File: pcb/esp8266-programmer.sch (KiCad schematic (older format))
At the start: 15 parts, among them P1 USB_OTG, P2 CONN_01X04, SW1 RESET, SW2 FLASH, SW3 SW_DP3T, U1 MCP1700T-3302E/TT, U1 MCP2221-I/SL

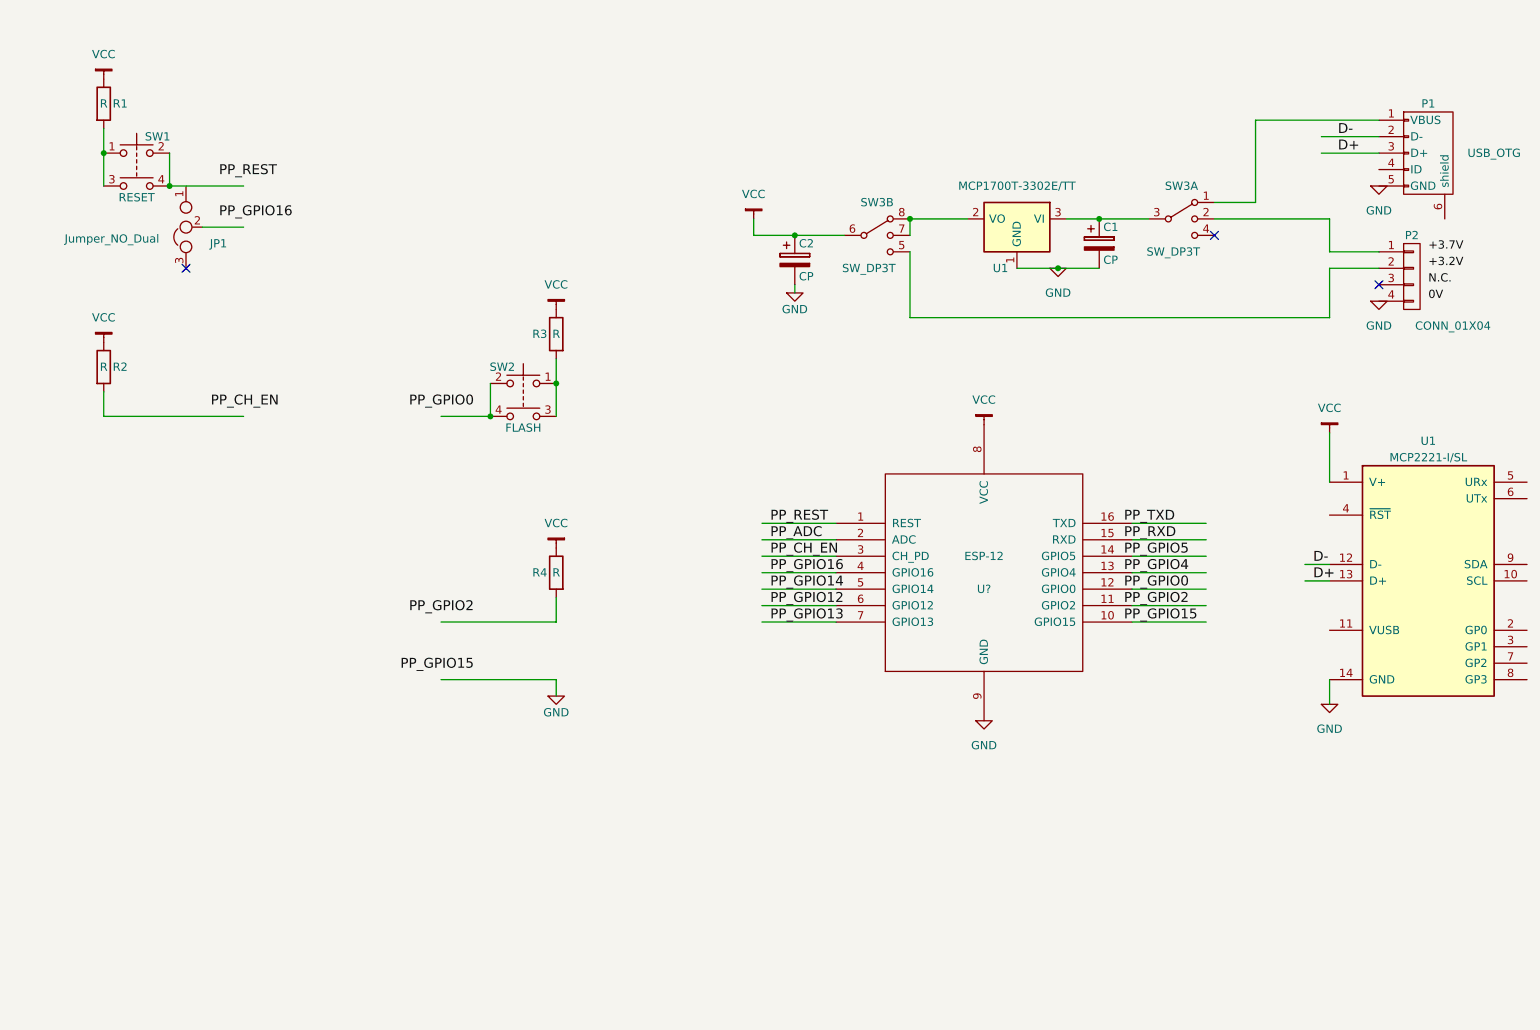
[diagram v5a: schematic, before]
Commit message: Fix wiring for switches. Add GPIO conns
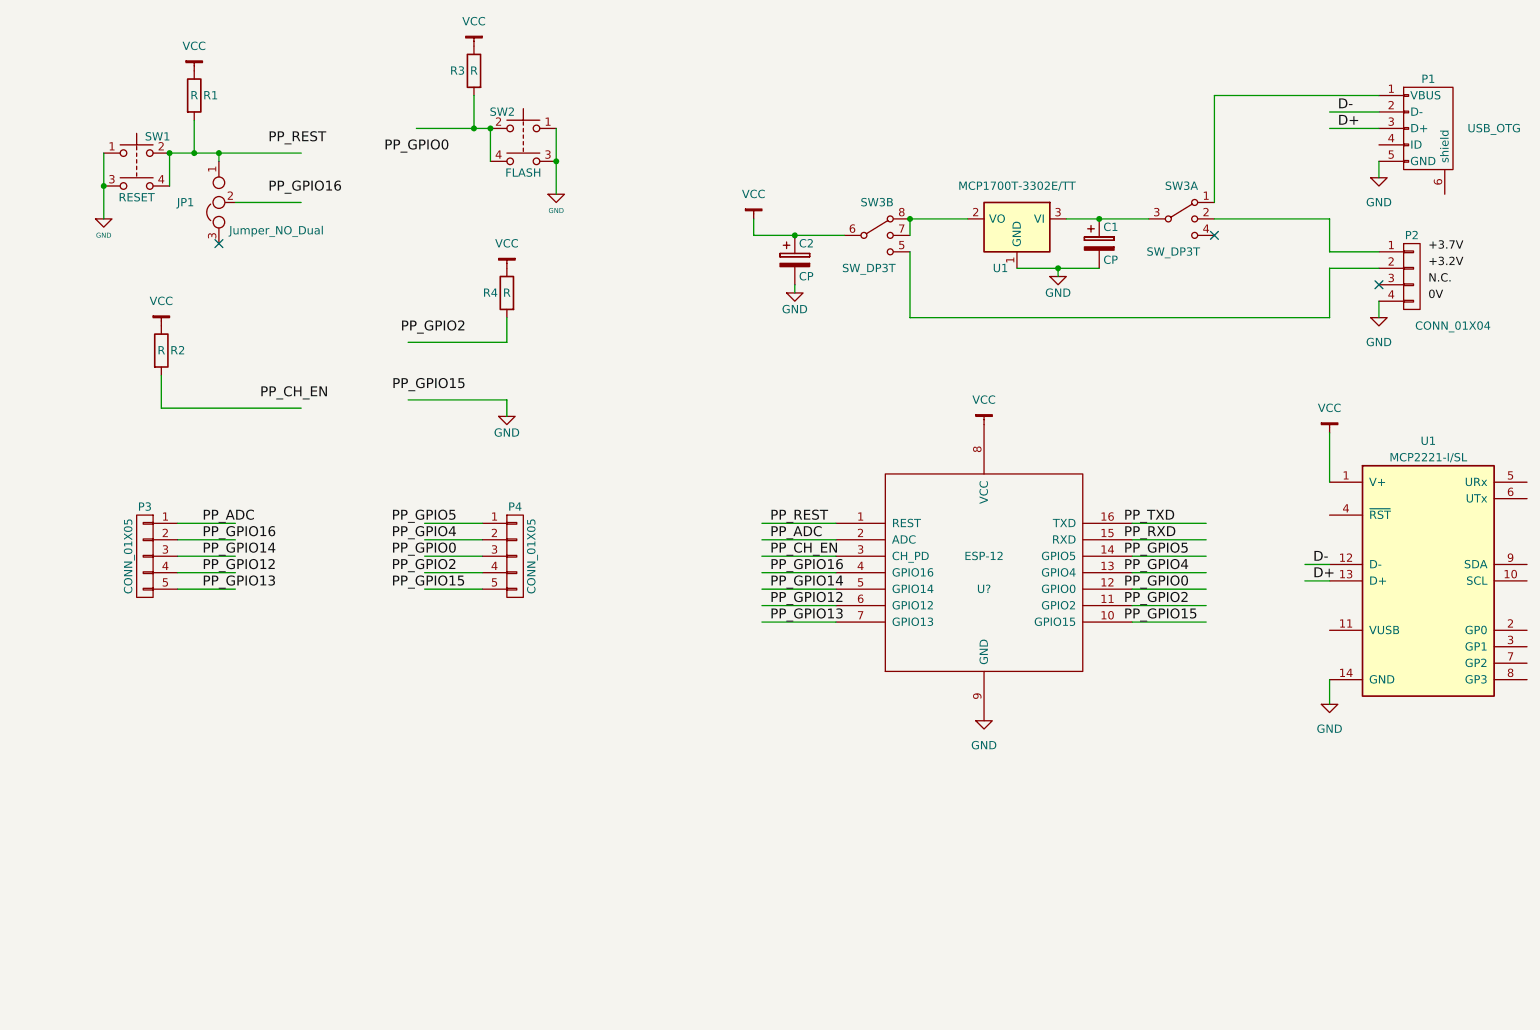
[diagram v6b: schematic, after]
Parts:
- added P3, P4: CONN_01X05, symbol CONN_01X05
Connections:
- wire segments 50 -> 73
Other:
- moved on the sheet: JP1, P1, R1, R2, R3, R4, SW2

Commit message: Add tri-state buffer parts
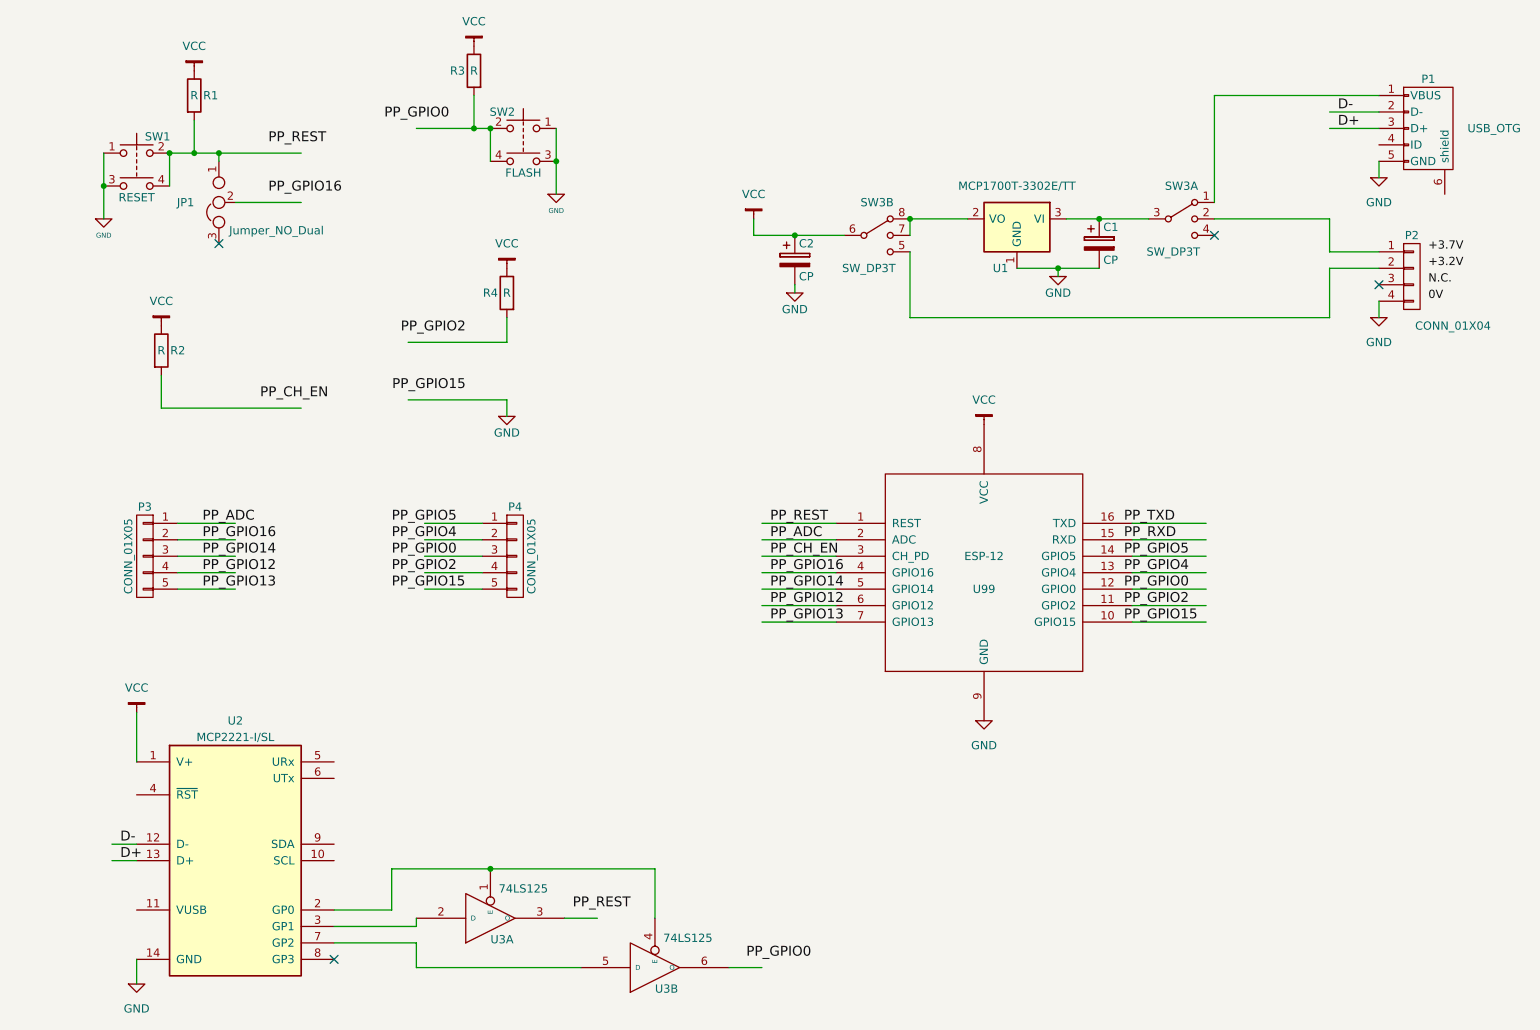
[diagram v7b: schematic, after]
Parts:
- added U3: 74LS125, symbol 74LS125
- gave numbers to parts that had none: 1
- renumbered U1 to U2
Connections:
- wire segments 73 -> 76
- no-connect marks 3 -> 4
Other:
- moved on the sheet: U2
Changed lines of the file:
@@
 	-1   0    0    -1
 $EndComp
-Text Label 3200 1650 2    60   ~ 0
+Text Label 3200 1450 2    60   ~ 0
 PP_GPIO0
 $Comp
@@
 PP_GPIO15
 $Comp
-L ESP-12 U?
+L ESP-12 U99
 U 1 1 58DFBEBA
 P 6450 4200
-F 0 "U?" H 6450 4100 50  0000 C CNN
+F 0 "U99" H 6450 4100 50  0000 C CNN
 F 1 "ESP-12" H 6450 4300 50  0000 C CNN
 F 2 "jdunmire/kicad-ESP8266/ESP8266.pretty:ESP-12" H 6450 4200 50  0001 C CNN
@@
 PP_GPIO15
 $Comp
-L MCP2221-I/SL U1
+L MCP2221-I/SL U2
 U 1 1 58DFCE15
-P 9150 4250
-F 0 "U1" H 9150 5100 50  0000 C CNN
-F 1 "MCP2221-I/SL" H 9150 5000 50  0000 C CNN
-F 2 "IPC7351-Nominal:SOIC127P600X175-14" H 9150 5000 60  0001 C CNN
-F 3 "http://ww1.microchip.com/downloads/en/DeviceDoc/20005292B.pdf" H 9150 5000 60  0001 C CNN
-F 4 "IC MICROCHIP MCP2221-I/SL" H 9650 5800 60  0001 C CNN "BOM"
-	1    9150 4250
+P 1900 5950
+F 0 "U2" H 1900 6800 50  0000 C CNN
+F 1 "MCP2221-I/SL" H 1900 6700 50  0000 C CNN
+F 2 "IPC7351-Nominal:SOIC127P600X175-14" H 1900 6700 60  0001 C CNN
+F 3 "http://ww1.microchip.com/downloads/en/DeviceDoc/20005292B.pdf" H 1900 6700 60  0001 C CNN
+F 4 "IC MICROCHIP MCP2221-I/SL" H 2400 7500 60  0001 C CNN "BOM"
+	1    1900 5950
 	1    0    0    -1
 $EndComp
@@
 Text Label 8600 1500 0    60   ~ 0
 D+
-Text Label 8450 4250 0    60   ~ 0
+Text Label 1200 5950 0    60   ~ 0
 D+
-Text Label 8450 4150 0    60   ~ 0
+Text Label 1200 5850 0    60   ~ 0
 D-
 $Comp
@@
 L VCC #PWR?
 U 1 1 58E06460
-P 8550 3350
-F 0 "#PWR?" H 8550 3200 50  0001 C CNN
-F 1 "VCC" H 8550 3500 50  0000 C CNN
-F 2 "" H 8550 3350 50  0000 C CNN
-F 3 "" H 8550 3350 50  0000 C CNN
-	1    8550 3350
+P 1300 5050
+F 0 "#PWR?" H 1300 4900 50  0001 C CNN
+F 1 "VCC" H 1300 5200 50  0000 C CNN
+F 2 "" H 1300 5050 50  0000 C CNN
+F 3 "" H 1300 5050 50  0000 C CNN
+	1    1300 5050
 	1    0    0    -1
 $EndComp
@@
 L GND-RESCUE-esp8266-programmer #PWR?
 U 1 1 58E064F7
-P 8550 5000
-F 0 "#PWR?" H 8550 4750 50  0001 C CNN
-F 1 "GND" H 8550 4850 50  0000 C CNN
-F 2 "" H 8550 5000 50  0000 C CNN
-F 3 "" H 8550 5000 50  0000 C CNN
-	1    8550 5000
+P 1300 6700
+F 0 "#PWR?" H 1300 6450 50  0001 C CNN
+F 1 "GND" H 1300 6550 50  0000 C CNN
+F 2 "" H 1300 6700 50  0000 C CNN
+F 3 "" H 1300 6700 50  0000 C CNN
+	1    1300 6700
 	1    0    0    -1
 $EndComp
@@
 	8550 2050 7850 2050
 Wire Wire Line
-	6950 2050 7150 2050
-Wire Wire Line
-	7150 2050 7450 2050
+	6950 2050 7450 2050
 Connection ~ 7150 2050
 Wire Wire Line
@@
 	6000 2050 6350 2050
 Wire Wire Line
-	6650 2350 6900 2350
-Wire Wire Line
-	6900 2350 7150 2350
-Wire Wire Line
-	5050 2150 5300 2150
-Wire Wire Line
-	5300 2150 5600 2150
+	6650 2350 7150 2350
+Wire Wire Line
+	5050 2150 5600 2150
 Wire Wire Line
 	5300 2450 5300 2500
@@
 Connection ~ 5300 2150
 Wire Wire Line
-	1100 1650 1100 1850
-Wire Wire Line
-	1100 1850 1100 2050
-Wire Wire Line
-	3000 1500 3350 1500
-Wire Wire Line
-	3350 1500 3450 1500
+	1100 1650 1100 2050
+Wire Wire Line
+	3000 1500 3450 1500
 Wire Wire Line
 	1450 3000 1450 3200
@@
 	7350 3900 7800 3900
 Wire Wire Line
-	8550 3650 8550 3350
+	1300 5350 1300 5050
 Wire Wire Line
 	8850 1400 8550 1400
@@
 	8850 1500 8550 1500
 Wire Wire Line
-	8550 4150 8400 4150
-Wire Wire Line
-	8550 4250 8400 4250
+	1300 5850 1150 5850
+Wire Wire Line
+	1300 5950 1150 5950
 Connection ~ 6900 2350
 Wire Wire Line
-	8550 4850 8550 5000
+	1300 6550 1300 6700
 Wire Wire Line
 	5050 2050 5050 2150
@@
 	8850 1700 8850 1800
 Wire Wire Line
-	3850 1500 3850 1700
-Wire Wire Line
-	3850 1700 3850 1900
+	3850 1500 3850 1900
 Connection ~ 3850 1700
 Connection ~ 1100 1850
@@
 	7850 1300 7850 1950
 Wire Wire Line
-	1500 1650 1650 1650
-Wire Wire Line
-	1650 1650 1800 1650
-Wire Wire Line
-	1800 1650 2300 1650
+	1500 1650 2300 1650
 Wire Wire Line
 	1500 1850 1500 1650
@@
 Wire Wire Line
 	3400 4300 3050 4300
+$Comp
+L 74LS125 U3
+U 1 1 58E6A14B
+P 3450 6300
+F 0 "U3" H 3450 6400 50  0000 L BNN
+F 1 "74LS125" H 3500 6150 50  0000 L TNN
+F 2 "" H 3450 6300 50  0000 C CNN
+F 3 "" H 3450 6300 50  0000 C CNN
+	1    3450 6300
+	1    0    0    1
+$EndComp
+$Comp
+L 74LS125 U3
+U 2 1 58E6B0B2
+P 4450 6600
+F 0 "U3" H 4450 6700 50  0000 L BNN
+F 1 "74LS125" H 4500 6450 50  0000 L TNN
+F 2 "" H 4450 6600 50  0000 C CNN
+F 3 "" H 4450 6600 50  0000 C CNN
+	2    4450 6600
+	1    0    0    1
+$EndComp
+Wire Wire Line
+	2500 6250 2850 6250
+Wire Wire Line
+	2850 6250 2850 6000
+Wire Wire Line
+	2850 6000 4450 6000
+Wire Wire Line
+	4450 6000 4450 6300
+Connection ~ 3450 6000
+Wire Wire Line
+	3000 6350 2500 6350
+Wire Wire Line
+	3000 6300 3000 6350
+Wire Wire Line
+	2500 6450 3000 6450
+Wire Wire Line
+	3000 6450 3000 6600
+Wire Wire Line
+	3000 6600 4000 6600
+Wire Wire Line
+	3900 6300 4100 6300
+Text Label 3950 6250 0    60   ~ 0
+PP_REST
+Wire Wire Line
+	4900 6600 5100 6600
+Text Label 5400 6550 2    60   ~ 0
+PP_GPIO0
+NoConn ~ 2500 6550
 $EndSCHEMATC

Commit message: Add tri-state buffers. Wire MCP2221
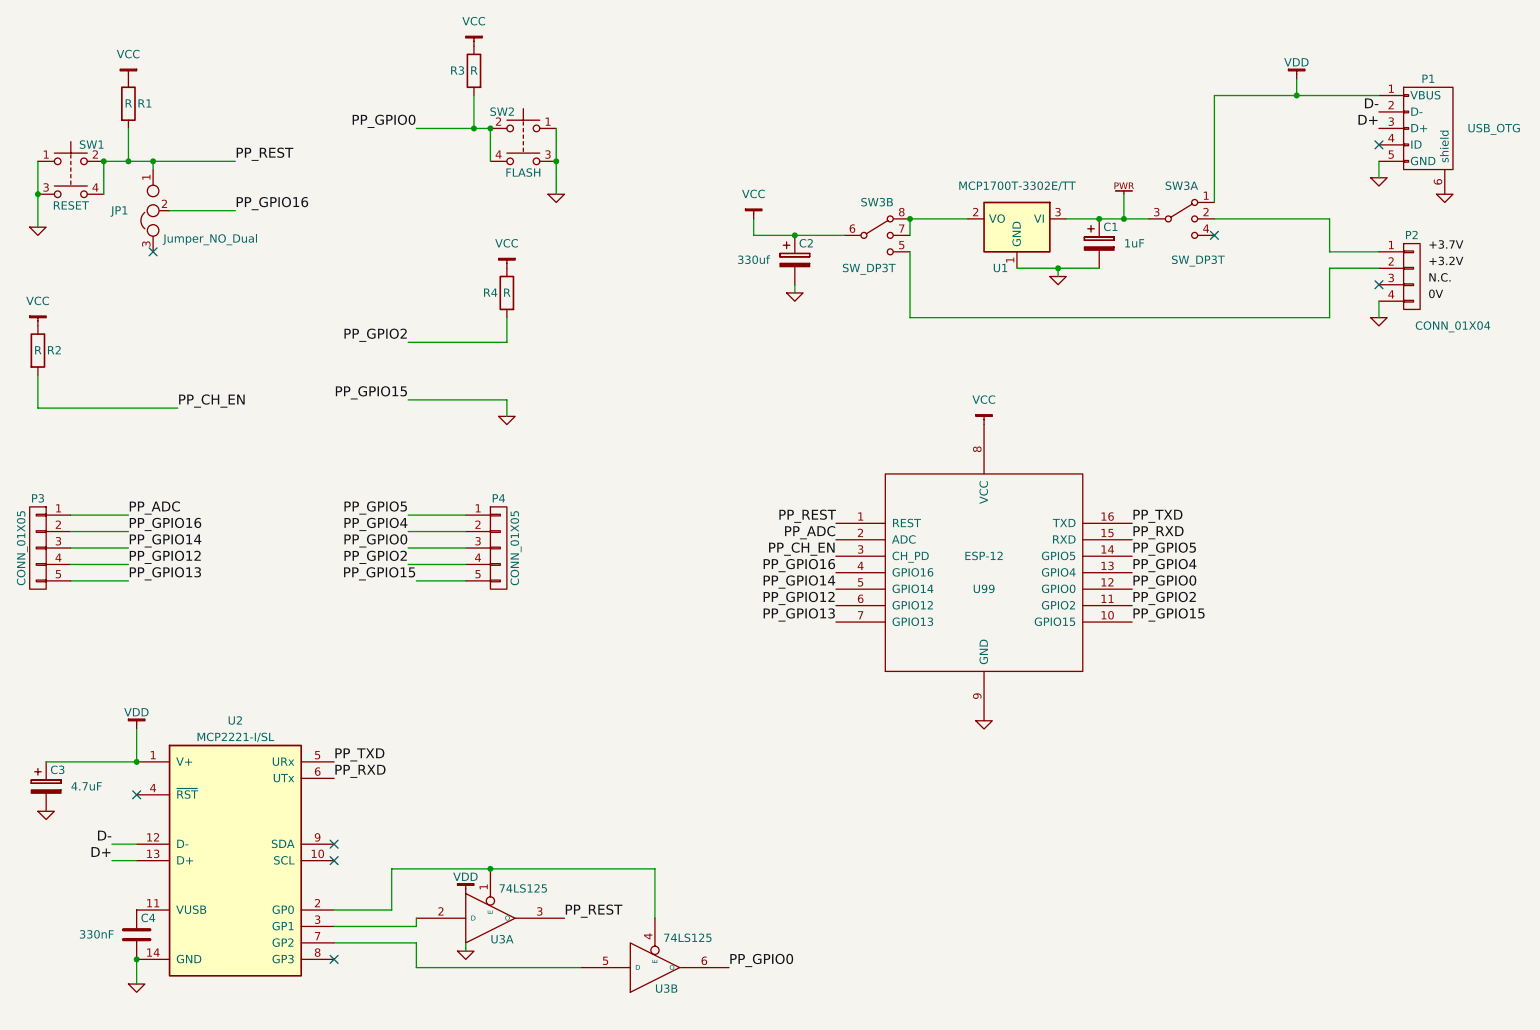
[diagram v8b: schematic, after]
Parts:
- added C3: 4.7uF, symbol CP
- added C4: 330nF, symbol C
- C1: value CP -> 1uF
- C2: value CP -> 330uf
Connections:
- net labels added: VDD
- wire segments 76 -> 62
- no-connect marks 4 -> 8
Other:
- moved on the sheet: JP1, P3, P4, R1, R2, SW1
